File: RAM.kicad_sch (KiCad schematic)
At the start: 31 parts, among them U1 H3, U7 MT41K512M16VRP-107 IT:P

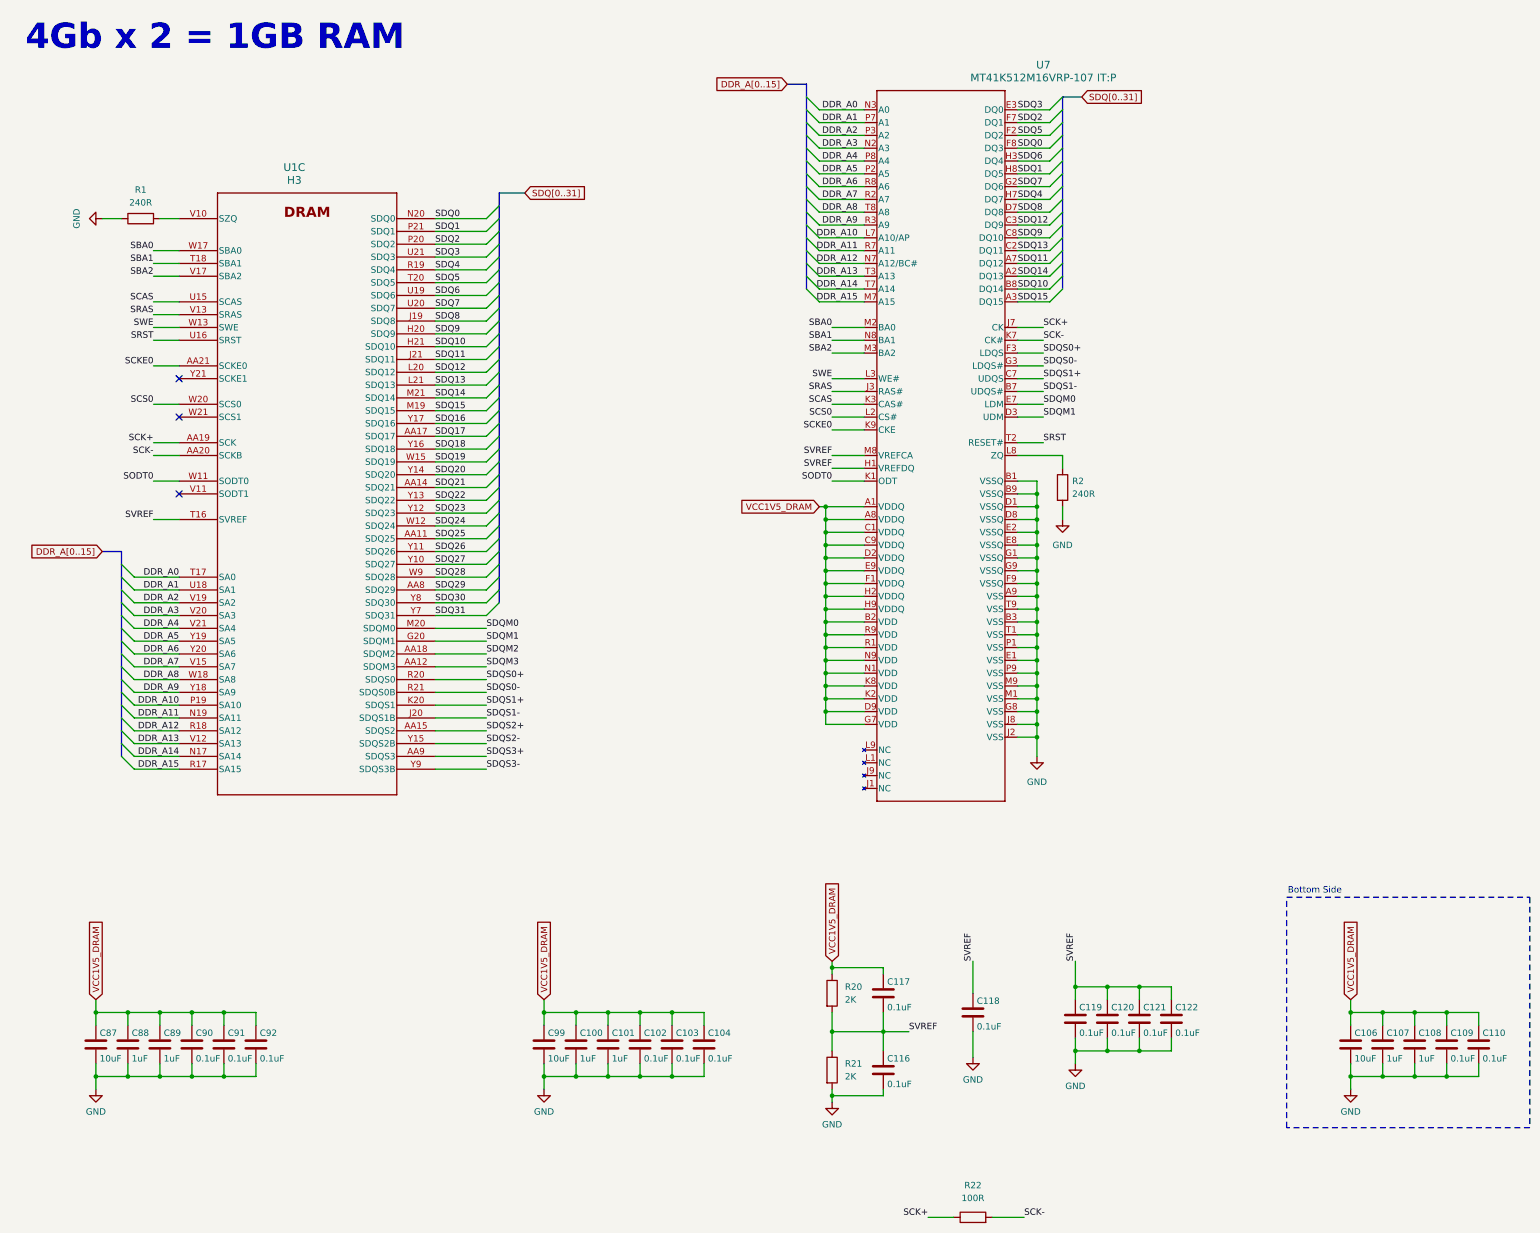
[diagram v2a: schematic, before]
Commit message: placed all decaps, emmc routing changes, DDR routing changes
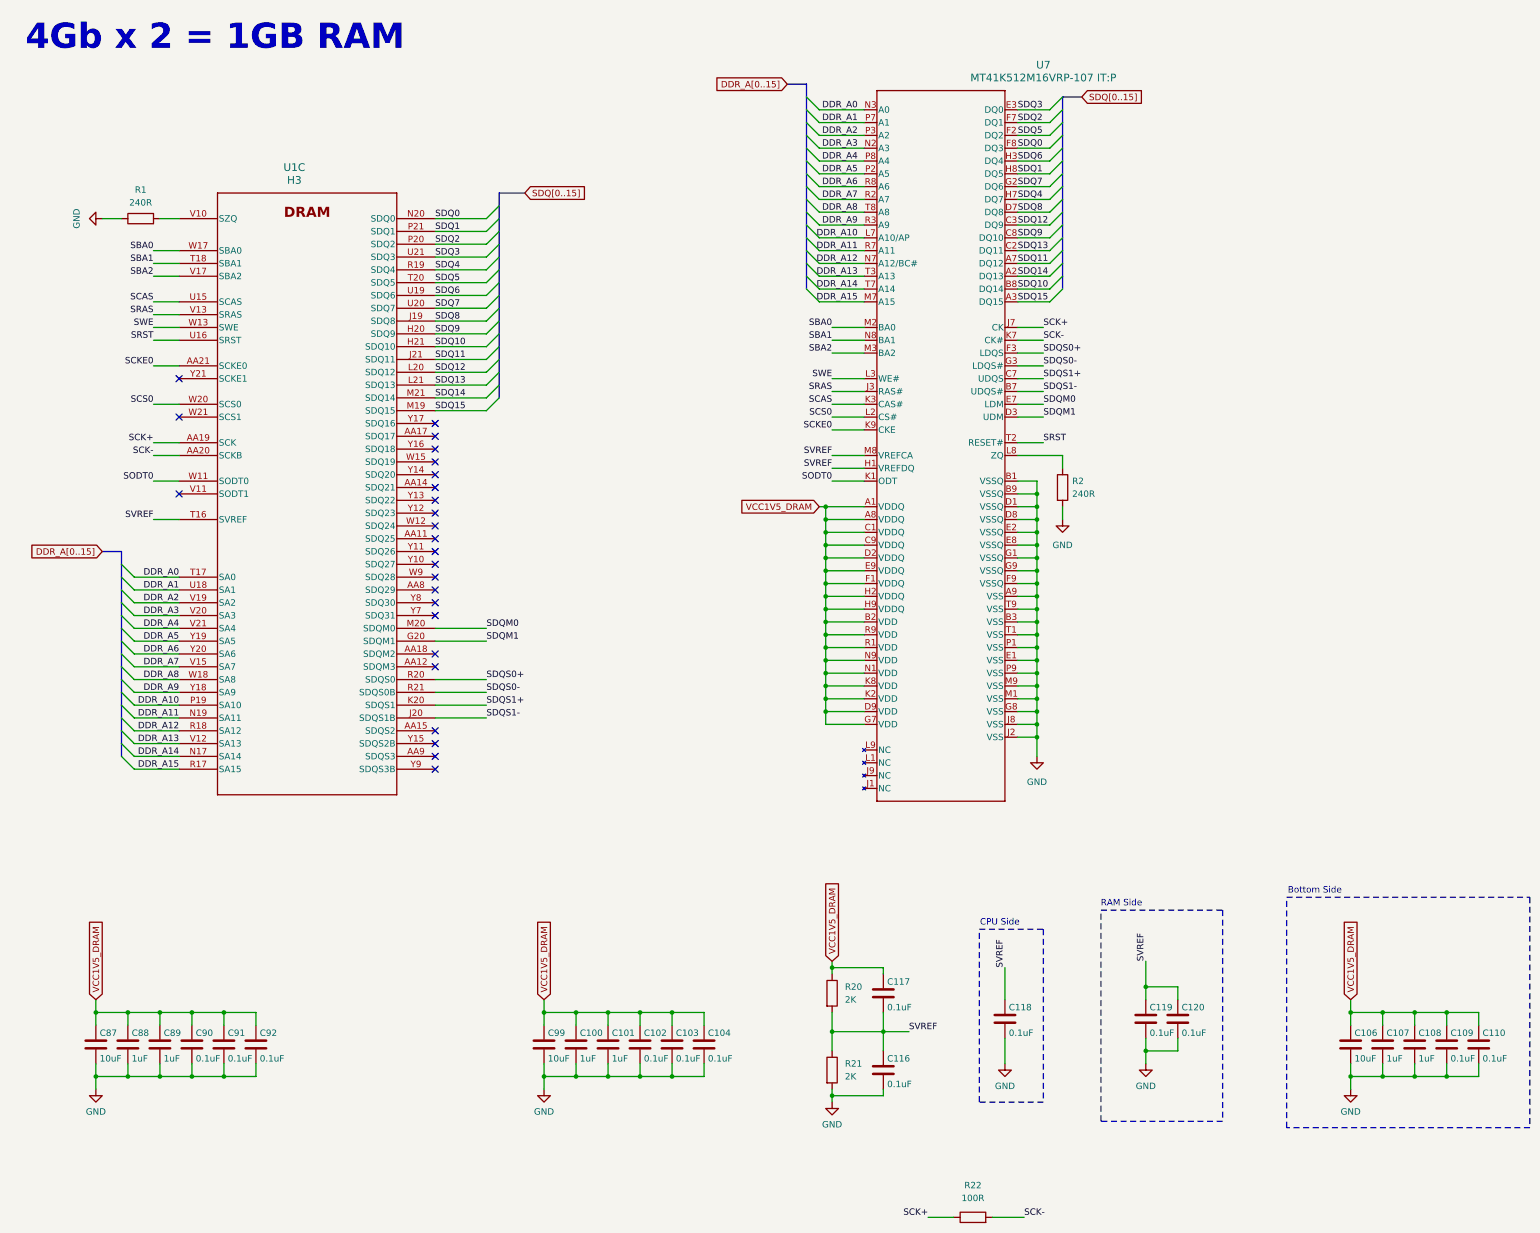
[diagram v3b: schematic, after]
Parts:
- removed C121, C122: 0.1uF, Capacitor_SMD:C_0402_1005Metric, symbol Device:C
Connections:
- net SDQ16: no longer names the net of U1.Y17 (SDQ16)
- net SDQ17: no longer names the net of U1.AA17 (SDQ17)
- net SDQ18: no longer names the net of U1.Y16 (SDQ18)
- net SDQ19: no longer names the net of U1.W15 (SDQ19)
- net SDQ20: no longer names the net of U1.Y14 (SDQ20)
- net SDQ21: no longer names the net of U1.AA14 (SDQ21)
- net SDQ22: no longer names the net of U1.Y13 (SDQ22)
- net SDQ23: no longer names the net of U1.Y12 (SDQ23)
- net SDQ24: no longer names the net of U1.W12 (SDQ24)
- net SDQ25: no longer names the net of U1.AA11 (SDQ25)
- net SDQ26: no longer names the net of U1.Y11 (SDQ26)
- net SDQ27: no longer names the net of U1.Y10 (SDQ27)
- net SDQ28: no longer names the net of U1.W9 (SDQ28)
- net SDQ29: no longer names the net of U1.AA8 (SDQ29)
- net SDQ30: no longer names the net of U1.Y8 (SDQ30)
- net SDQ31: no longer names the net of U1.Y7 (SDQ31)
- net SDQM2: no longer names the net of U1.AA18 (SDQM2)
- net SDQM3: no longer names the net of U1.AA12 (SDQM3)
- net SDQS2+: no longer names the net of U1.AA15 (SDQS2)
- net SDQS2-: no longer names the net of U1.Y15 (SDQS2B)
- net SDQS3+: no longer names the net of U1.AA9 (SDQS3)
- net SDQS3-: no longer names the net of U1.Y9 (SDQS3B)
- no-connect marks 3 -> 25
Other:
- note added: "CPU Side"
- note added: "RAM Side"
- moved on the sheet: C118, C119, C120
